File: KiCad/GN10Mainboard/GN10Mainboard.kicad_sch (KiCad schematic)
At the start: 129 parts, among them J1 USB_C_Receptacle_USB2.0_16P, J2 Conn_01x04, J3 Conn_01x04, J4 USB_C_Receptacle_USB2.0_16P, J5 Conn_01x04, J6 Conn_01x06, J7 Conn_01x04, J8 Conn_01x04, J9 XT30PW-M, SW1 SW_DIP_x04, SW2 SW_Push, SW3 SW_Push, SW4 SW_Push, SW5 SW_Push, U1 STM32G474RCTx, U10 3.3V, U2 FT231XS, U3 RNBD451, U4 FT231XS, U5 MCP2562-E-SN, U6 MCP2562-E-SN, U7 BNO055, U8 7segmentLED, U9 OKL-T/x-W5N-C, Y1 32.768kHz, Y2 24MHz, Y3 Crystal

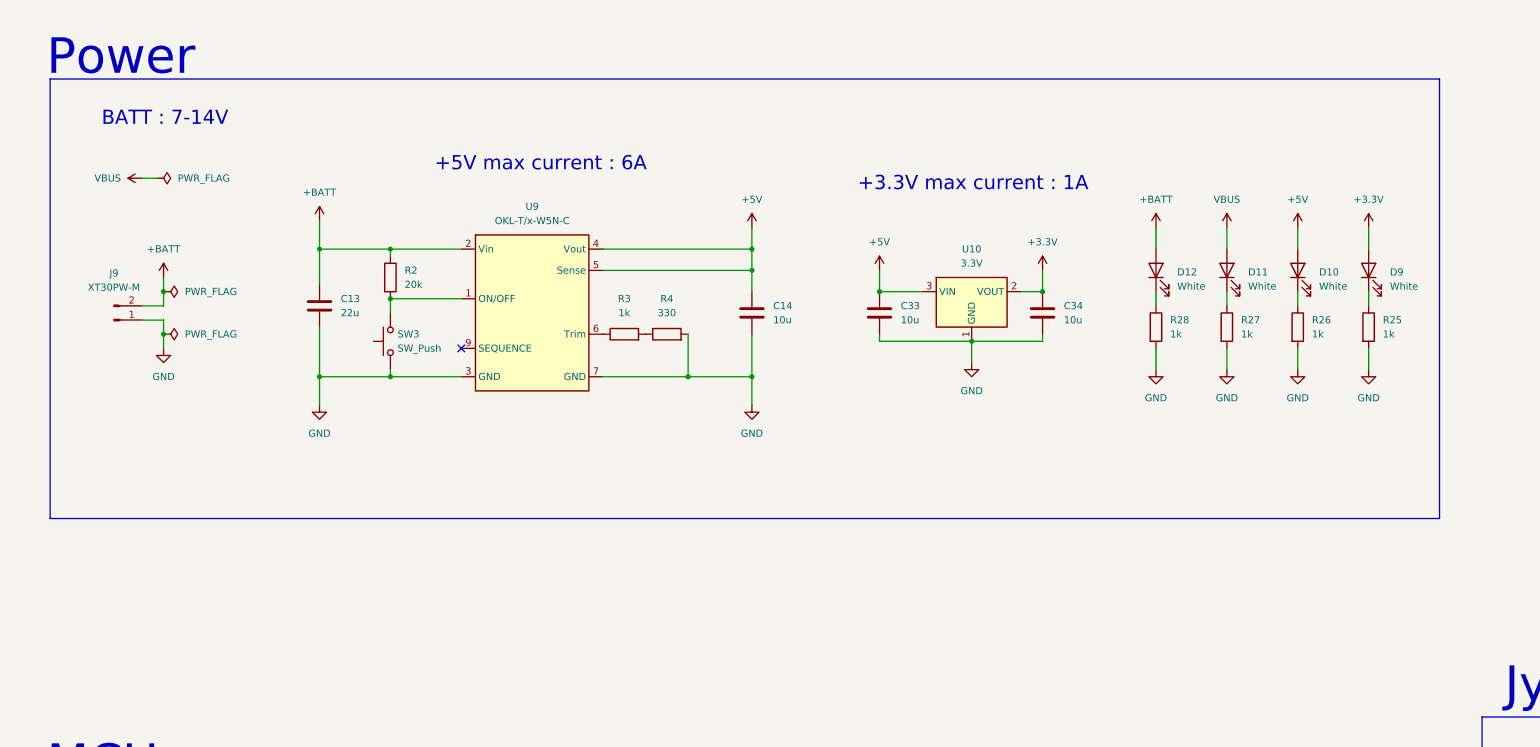
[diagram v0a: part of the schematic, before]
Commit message: add: USB power supply switch for 5V.
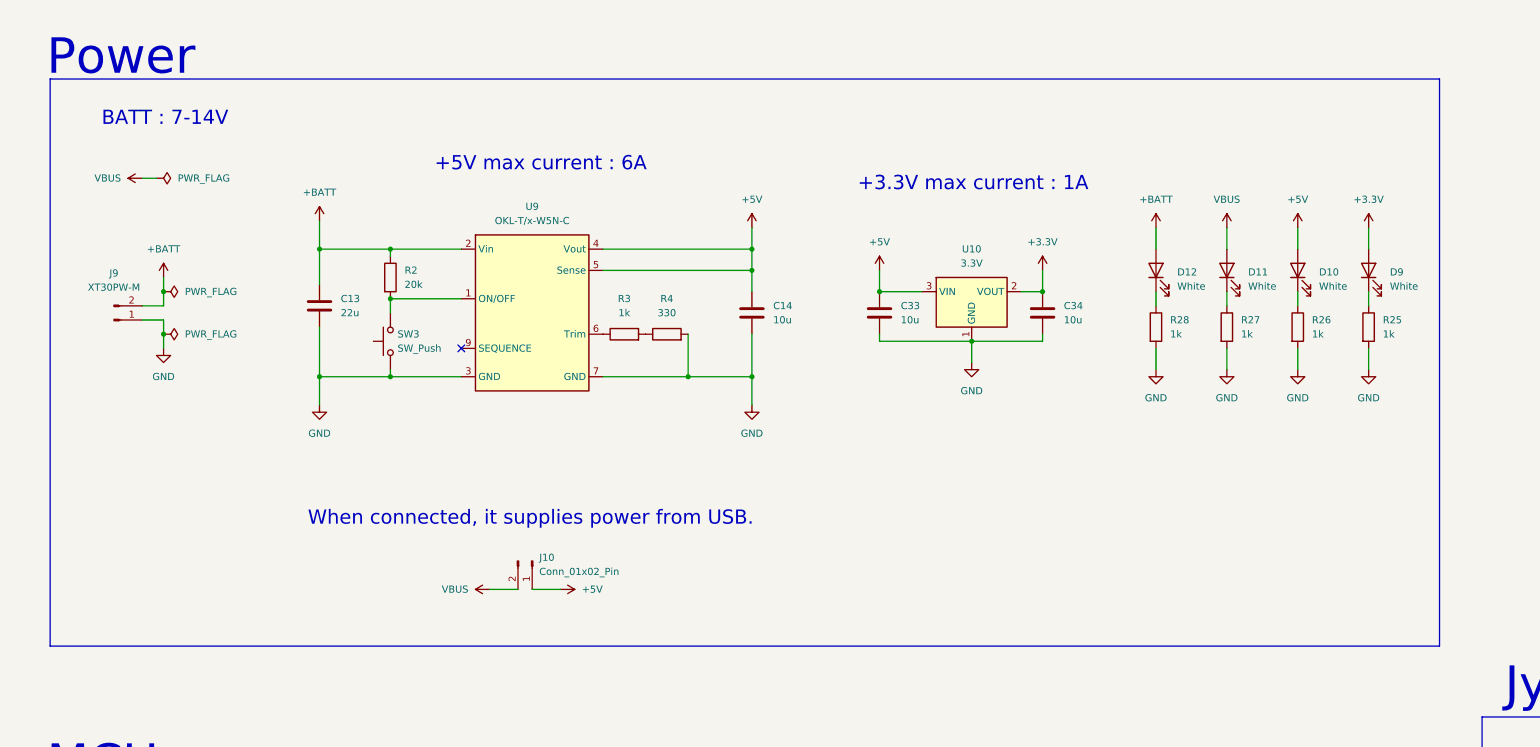
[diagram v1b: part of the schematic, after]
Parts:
- added J10: Conn_01x02_Pin, symbol Connector:Conn_01x02_Pin
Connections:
- net +5V: now also J10.1 (Pin_1)
- net VBUS: now also J10.2 (Pin_2)
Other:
- note added: "When connected, it supplies power from USB."
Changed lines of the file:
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@@
 	(wire
 		(pts
+			(xy 104.14 116.84) (xy 109.22 116.84)
+		)
+		(stroke
+			(width 0)
+			(type default)
+		)
+	)
+	(wire
+		(pts
 			(xy 118.11 171.45) (xy 128.27 171.45)
 		)
@@
 	(wire
 		(pts
+			(xy 111.76 116.84) (xy 116.84 116.84)
+		)
+		(stroke
+			(width 0)
+			(type default)
+		)
+	)
+	(wire
+		(pts
 			(xy 304.8 175.26) (xy 304.8 173.99)
 		)
@@
 	(rectangle
 		(start 25.4 25.4)
-		(end 274.32 104.14)
+		(end 274.32 127)
 		(stroke
 			(width 0)
@@
 		)
 	)
+	(text "When connected, it supplies power from USB."
+		(exclude_from_sim no)
+		(at 111.506 104.14 0)
+		(effects
+			(font
+				(size 2.54 2.54)
+			)
+		)
+	)
 	(text "MCU"
 		(exclude_from_sim no)
@@
 	)
 	(symbol
+		(lib_id "power:VBUS")
+		(at 104.14 116.84 90)
+		(unit 1)
+		(exclude_from_sim no)
+		(in_bom yes)
+		(on_board yes)
+		(dnp no)
+		(fields_autoplaced yes)
+		(property "Reference" "#PWR094"
+			(at 107.95 116.84 0)
+			(effects
+				(font
+					(size 1.27 1.27)
+				)
+				(hide yes)
+			)
+		)
+		(property "Value" "VBUS"
+			(at 100.33 116.8399 90)
+			(effects
+				(font
+					(size 1.27 1.27)
+				)
+				(justify left)
+			)
+		)
+		(property "Footprint" ""
+			(at 104.14 116.84 0)
+			(effects
+				(font
+					(size 1.27 1.27)
+				)
+				(hide yes)
+			)
+		)
+		(property "Datasheet" ""
+			(at 104.14 116.84 0)
+			(effects
+				(font
+					(size 1.27 1.27)
+				)
+				(hide yes)
+			)
+		)
+		(property "Description" "Power symbol creates a global label with name \"VBUS\""
+			(at 104.14 116.84 0)
+			(effects
+				(font
+					(size 1.27 1.27)
+				)
+				(hide yes)
+			)
+		)
+		(pin "1"
+		)
+		(instances
+			(project "GN10Mainboard"
+				(path "/b58ae320-37f1-47e7-bf16-145390e42e75"
+					(reference "#PWR094")
+					(unit 1)
+				)
+			)
+		)
+	)
+	(symbol
 		(lib_id "Device:LED")
 		(at 534.67 69.85 90)
@@
 	)
 	(symbol
+		(lib_id "Connector:Conn_01x02_Pin")
+		(at 111.76 111.76 270)
+		(unit 1)
+		(exclude_from_sim no)
+		(in_bom yes)
+		(on_board yes)
+		(dnp no)
+		(fields_autoplaced yes)
+		(property "Reference" "J10"
+			(at 113.03 111.1249 90)
+			(effects
+				(font
+					(size 1.27 1.27)
+				)
+				(justify left)
+			)
+		)
+		(property "Value" "Conn_01x02_Pin"
+			(at 113.03 113.6649 90)
+			(effects
+				(font
+					(size 1.27 1.27)
+				)
+				(justify left)
+			)
+		)
+		(property "Footprint" ""
+			(at 111.76 111.76 0)
+			(effects
+				(font
+					(size 1.27 1.27)
+				)
+				(hide yes)
+			)
+		)
+		(property "Datasheet" "~"
+			(at 111.76 111.76 0)
+			(effects
+				(font
+					(size 1.27 1.27)
+				)
+				(hide yes)
+			)
+		)
+		(property "Description" "Generic connector, single row, 01x02, script generated"
+			(at 111.76 111.76 0)
+			(effects
+				(font
+					(size 1.27 1.27)
+				)
+				(hide yes)
+			)
+		)
+		(pin "2"
+		)
+		(pin "1"
+		)
+		(instances
+			(project ""
+				(path "/b58ae320-37f1-47e7-bf16-145390e42e75"
+					(reference "J10")
+					(unit 1)
+				)
+			)
+		)
+	)
+	(symbol
 		(lib_id "power:GND")
 		(at 304.8 187.96 0)
@@
 					(unit 1)
 				)
+			)
+		)
+	)
+	(symbol
+		(lib_id "power:+5V")
+		(at 116.84 116.84 270)
+		(unit 1)
+		(exclude_from_sim no)
+		(in_bom yes)
+		(on_board yes)
+		(dnp no)
+		(fields_autoplaced yes)
+		(property "Reference" "#PWR095"
+			(at 113.03 116.84 0)
+			(effects
+				(font
+					(size 1.27 1.27)
+				)
+				(hide yes)
+			)
+		)
+		(property "Value" "+5V"
+			(at 120.65 116.8399 90)
+			(effects
+				(font
+					(size 1.27 1.27)
+				)
+				(justify left)
+			)
+		)
+		(property "Footprint" ""
+			(at 116.84 116.84 0)
+			(effects
+				(font
+					(size 1.27 1.27)
+				)
+				(hide yes)
+			)
+		)
+		(property "Datasheet" ""
+			(at 116.84 116.84 0)
+			(effects
+				(font
+					(size 1.27 1.27)
+				)
+				(hide yes)
+			)
+		)
+		(property "Description" "Power symbol creates a global label with name \"+5V\""
+			(at 116.84 116.84 0)
+			(effects
+				(font
+					(size 1.27 1.27)
+				)
+				(hide yes)
+			)
+		)
+		(pin "1"
+		)
+		(instances
+			(project "GN10Mainboard"
+				(path "/b58ae320-37f1-47e7-bf16-145390e42e75"
+					(reference "#PWR095")
+					(unit 1)
+				)

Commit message: fix: around DCDC convertor
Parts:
- removed SW3: SW_Push, symbol Switch:SW_Push
- added D17: SS2040FL, symbol Device:D
- added JP14: Jumper_2_Open, symbol Jumper:Jumper_2_Open
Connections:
- net +5V: now also D17.2 (A)
- net +BATT: now also D17.1 (K)
- net GND: now also JP14.1 (A)
- net at R2.2, U9.1 (ON/OFF): now also JP14.2 (B)
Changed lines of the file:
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@@
 	)
 	(junction
+		(at 73.66 44.45)
+		(diameter 0)
+		(color 0 0 0 0)
+	)
+	(junction
 		(at 469.9 238.76)
 		(diameter 0)
@@
 	)
 	(junction
+		(at 151.13 44.45)
+		(diameter 0)
+		(color 0 0 0 0)
+	)
+	(junction
 		(at 359.41 246.38)
 		(diameter 0)
@@
 	(wire
 		(pts
+			(xy 73.66 44.45) (xy 107.95 44.45)
+		)
+		(stroke
+			(width 0)
+			(type default)
+		)
+	)
+	(wire
+		(pts
 			(xy 419.1 361.95) (xy 431.8 361.95)
 		)
@@
 	(wire
 		(pts
+			(xy 73.66 44.45) (xy 73.66 55.88)
+		)
+		(stroke
+			(width 0)
+			(type default)
+		)
+	)
+	(wire
+		(pts
 			(xy 275.59 369.57) (xy 275.59 351.79)
 		)
@@
 	(wire
 		(pts
-			(xy 73.66 50.8) (xy 73.66 55.88)
+			(xy 73.66 40.64) (xy 73.66 44.45)
 		)
 		(stroke
@@
 	(wire
 		(pts
+			(xy 151.13 44.45) (xy 151.13 55.88)
+		)
+		(stroke
+			(width 0)
+			(type default)
+		)
+	)
+	(wire
+		(pts
 			(xy 391.16 269.24) (xy 391.16 270.51)
 		)
@@
 	(wire
 		(pts
+			(xy 115.57 44.45) (xy 151.13 44.45)
+		)
+		(stroke
+			(width 0)
+			(type default)
+		)
+	)
+	(wire
+		(pts
 			(xy 466.09 260.35) (xy 467.36 260.35)
 		)
@@
 	(wire
 		(pts
-			(xy 151.13 52.07) (xy 151.13 55.88)
+			(xy 151.13 40.64) (xy 151.13 44.45)
 		)
 		(stroke
@@
 	(text "+5V max current : 6A"
 		(exclude_from_sim no)
-		(at 113.284 40.64 0)
+		(at 112.014 31.242 0)
 		(effects
 			(font
@@
 	)
 	(symbol
-		(lib_id "Switch:SW_Push")
-		(at 86.36 72.39 90)
-		(unit 1)
-		(exclude_from_sim no)
-		(in_bom yes)
-		(on_board yes)
-		(dnp no)
-		(property "Reference" "SW3"
-			(at 87.63 71.1199 90)
-			(effects
-				(font
-					(size 1.27 1.27)
-				)
-				(justify right)
-			)
-		)
-		(property "Value" "SW_Push"
-			(at 87.63 73.6599 90)
-			(effects
-				(font
-					(size 1.27 1.27)
-				)
-				(justify right)
-			)
-		)
-		(property "Footprint" ""
-			(at 81.28 72.39 0)
-			(effects
-				(font
-					(size 1.27 1.27)
-				)
-				(hide yes)
-			)
-		)
-		(property "Datasheet" "~"
-			(at 81.28 72.39 0)
-			(effects
-				(font
-					(size 1.27 1.27)
-				)
-				(hide yes)
-			)
-		)
-		(property "Description" "Push button switch, generic, two pins"
-			(at 86.36 72.39 0)
-			(effects
-				(font
-					(size 1.27 1.27)
-				)
-				(hide yes)
-			)
-		)
-		(pin "2"
-		)
-		(pin "1"
-		)
-		(instances
-			(project ""
-				(path "/b58ae320-37f1-47e7-bf16-145390e42e75"
-					(reference "SW3")
-					(unit 1)
-				)
-			)
-		)
-	)
-	(symbol
 		(lib_id "Device:C")
 		(at 356.87 82.55 0)
@@
 	(symbol
 		(lib_id "power:+5V")
-		(at 151.13 52.07 0)
+		(at 151.13 40.64 0)
 		(unit 1)
 		(exclude_from_sim no)
@@
 		(fields_autoplaced yes)
 		(property "Reference" "#PWR022"
-			(at 151.13 55.88 0)
+			(at 151.13 44.45 0)
 			(effects
 				(font
@@
 		)
 		(property "Value" "+5V"
-			(at 151.13 46.99 0)
+			(at 151.13 35.56 0)
 			(effects
 				(font
@@
 		)
 		(property "Footprint" ""
-			(at 151.13 52.07 0)
+			(at 151.13 40.64 0)
 			(effects
 				(font
@@
 		)
 		(property "Datasheet" ""
-			(at 151.13 52.07 0)
+			(at 151.13 40.64 0)
 			(effects
 				(font
@@
 		)
 		(property "Description" "Power symbol creates a global label with name \"+5V\""
-			(at 151.13 52.07 0)
+			(at 151.13 40.64 0)
 			(effects
 				(font
@@
 	)
 	(symbol
+		(lib_id "Jumper:Jumper_2_Open")
+		(at 86.36 72.39 90)
+		(unit 1)
+		(exclude_from_sim yes)
+		(in_bom yes)
+		(on_board yes)
+		(dnp no)
+		(fields_autoplaced yes)
+		(property "Reference" "JP14"
+			(at 87.63 71.1199 90)
+			(effects
+				(font
+					(size 1.27 1.27)
+				)
+				(justify right)
+			)
+		)
+		(property "Value" "Jumper_2_Open"
+			(at 87.63 73.6599 90)
+			(effects
+				(font
+					(size 1.27 1.27)
+				)
+				(justify right)
+				(hide yes)
+			)
+		)
+		(property "Footprint" ""
+			(at 86.36 72.39 0)
+			(effects
+				(font
+					(size 1.27 1.27)
+				)
+				(hide yes)
+			)
+		)
+		(property "Datasheet" "~"
+			(at 86.36 72.39 0)
+			(effects
+				(font
+					(size 1.27 1.27)
+				)
+				(hide yes)
+			)
+		)
+		(property "Description" "Jumper, 2-pole, open"
+			(at 86.36 72.39 0)
+			(effects
+				(font
+					(size 1.27 1.27)
+				)
+				(hide yes)
+			)
+		)
+		(pin "2"
+		)
+		(pin "1"
+		)
+		(instances
+			(project "GN10Mainboard"
+				(path "/b58ae320-37f1-47e7-bf16-145390e42e75"
+					(reference "JP14")
+					(unit 1)
+				)
+			)
+		)
+	)
+	(symbol
 		(lib_id "Jumper:SolderJumper_2_Open")
 		(at 488.95 182.88 0)
@@
 	(symbol
 		(lib_id "power:+BATT")
-		(at 73.66 50.8 0)
+		(at 73.66 40.64 0)
 		(unit 1)
 		(exclude_from_sim no)
@@
 		(fields_autoplaced yes)
 		(property "Reference" "#PWR020"
-			(at 73.66 54.61 0)
+			(at 73.66 44.45 0)
 			(effects
 				(font
@@
 		)
 		(property "Value" "+BATT"
-			(at 73.66 45.72 0)
+			(at 73.66 35.56 0)
 			(effects
 				(font
@@
 		)
 		(property "Footprint" ""
-			(at 73.66 50.8 0)
+			(at 73.66 40.64 0)
 			(effects
 				(font
@@
 		)
 		(property "Datasheet" ""
-			(at 73.66 50.8 0)
+			(at 73.66 40.64 0)
 			(effects
 				(font
@@
 		)
 		(property "Description" "Power symbol creates a global label with name \"+BATT\""
-			(at 73.66 50.8 0)
+			(at 73.66 40.64 0)
 			(effects
 				(font
@@
 					(unit 1)
 				)
+			)
+		)
+	)
+	(symbol
+		(lib_id "Device:D")
+		(at 111.76 44.45 0)
+		(unit 1)
+		(exclude_from_sim no)
+		(in_bom yes)
+		(on_board yes)
+		(dnp no)
+		(fields_autoplaced yes)
+		(property "Reference" "D17"
+			(at 111.76 38.1 0)
+			(effects
+				(font
+					(size 1.27 1.27)
+				)
+			)
+		)
+		(property "Value" "SS2040FL"
+			(at 111.76 40.64 0)
+			(effects
+				(font
+					(size 1.27 1.27)
+				)
+			)
+		)
+		(property "Footprint" ""
+			(at 111.76 44.45 0)
+			(effects
+				(font
+					(size 1.27 1.27)
+				)
+				(hide yes)
+			)
+		)
+		(property "Datasheet" "~"
+			(at 111.76 44.45 0)
+			(effects
+				(font
+					(size 1.27 1.27)
+				)
+				(hide yes)
+			)
+		)
+		(property "Description" "Diode"
+			(at 111.76 44.45 0)
+			(effects
+				(font
+					(size 1.27 1.27)
+				)
+				(hide yes)
+			)
+		)
+		(property "Sim.Device" "D"
+			(at 111.76 44.45 0)
+			(effects
+				(font
+					(size 1.27 1.27)
+				)
+				(hide yes)
+			)
+		)
+		(property "Sim.Pins" "1=K 2=A"
+			(at 111.76 44.45 0)
+			(effects
+				(font
+					(size 1.27 1.27)
+				)
+				(hide yes)
+			)
+		)
+		(pin "2"
+		)
+		(pin "1"
+		)
+		(instances
+			(project ""
+				(path "/b58ae320-37f1-47e7-bf16-145390e42e75"
+					(reference "D17")
+					(unit 1)
+				)

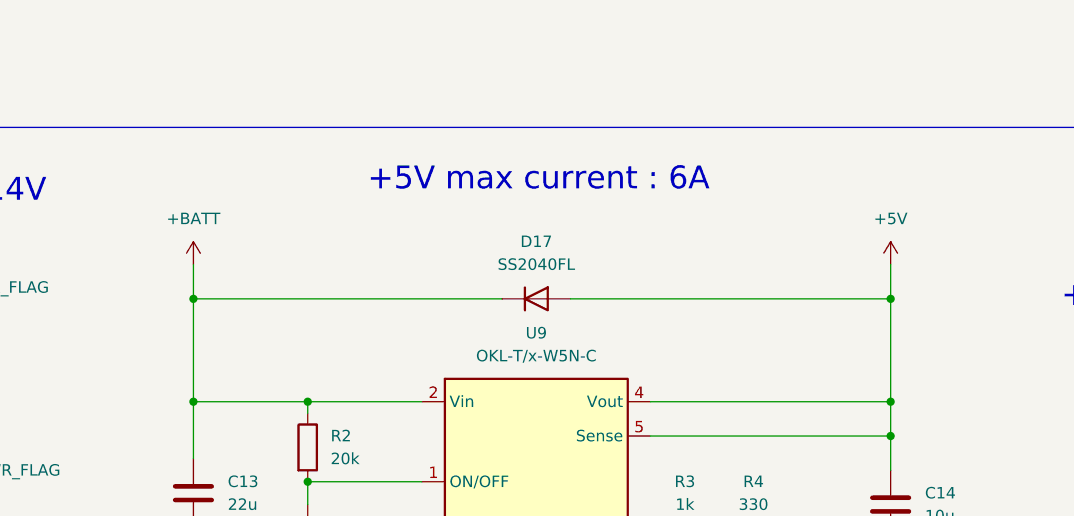
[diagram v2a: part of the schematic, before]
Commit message: The DCDC does not require a reverse voltage protection diode, so I removed it.
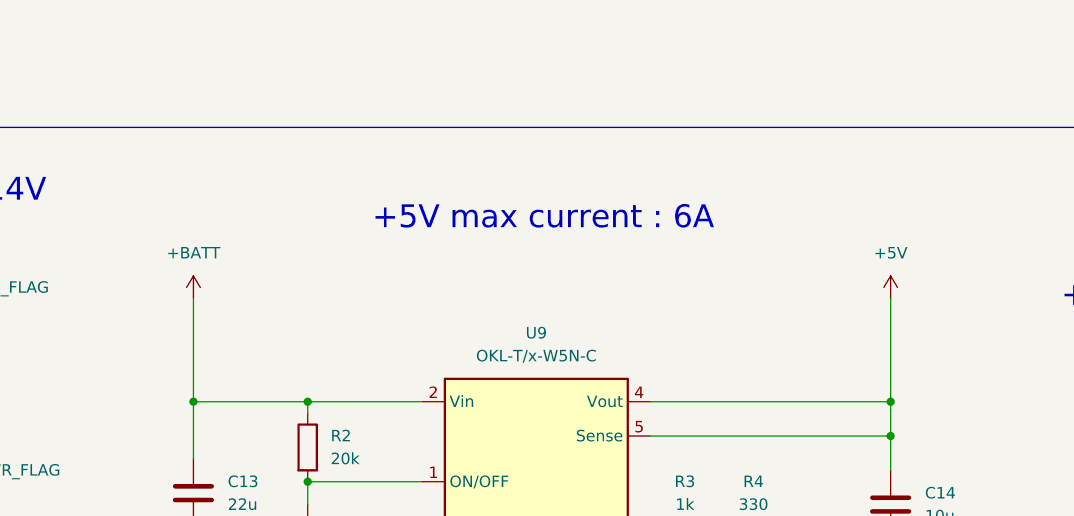
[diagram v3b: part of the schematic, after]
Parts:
- removed D17: SS2040FL, symbol Device:D
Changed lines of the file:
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@@
 	)
 	(junction
-		(at 73.66 44.45)
-		(diameter 0)
-		(color 0 0 0 0)
-	)
-	(junction
 		(at 469.9 238.76)
 		(diameter 0)
@@
 	)
 	(junction
-		(at 151.13 44.45)
-		(diameter 0)
-		(color 0 0 0 0)
-	)
-	(junction
 		(at 359.41 246.38)
 		(diameter 0)
@@
 	(wire
 		(pts
-			(xy 73.66 44.45) (xy 107.95 44.45)
-		)
-		(stroke
-			(width 0)
-			(type default)
-		)
-	)
-	(wire
-		(pts
 			(xy 419.1 361.95) (xy 431.8 361.95)
 		)
@@
 	(wire
 		(pts
-			(xy 73.66 40.64) (xy 73.66 44.45)
-		)
-		(stroke
-			(width 0)
-			(type default)
-		)
-	)
-	(wire
-		(pts
 			(xy 491.49 260.35) (xy 494.03 260.35)
 		)
@@
 	(wire
 		(pts
-			(xy 115.57 44.45) (xy 151.13 44.45)
-		)
-		(stroke
-			(width 0)
-			(type default)
-		)
-	)
-	(wire
-		(pts
 			(xy 466.09 260.35) (xy 467.36 260.35)
 		)
@@
 	(wire
 		(pts
-			(xy 151.13 40.64) (xy 151.13 44.45)
-		)
-		(stroke
-			(width 0)
-			(type default)
-		)
-	)
-	(wire
-		(pts
 			(xy 466.09 236.22) (xy 466.09 238.76)
 		)
@@
 	(text "+5V max current : 6A"
 		(exclude_from_sim no)
-		(at 112.014 31.242 0)
+		(at 112.522 35.56 0)
 		(effects
 			(font
@@
 	(symbol
 		(lib_id "power:+5V")
-		(at 151.13 40.64 0)
+		(at 151.13 44.45 0)
 		(unit 1)
 		(exclude_from_sim no)
@@
 		(fields_autoplaced yes)
 		(property "Reference" "#PWR022"
-			(at 151.13 44.45 0)
+			(at 151.13 48.26 0)
 			(effects
 				(font
@@
 		)
 		(property "Value" "+5V"
-			(at 151.13 35.56 0)
+			(at 151.13 39.37 0)
 			(effects
 				(font
@@
 		)
 		(property "Footprint" ""
-			(at 151.13 40.64 0)
+			(at 151.13 44.45 0)
 			(effects
 				(font
@@
 		)
 		(property "Datasheet" ""
-			(at 151.13 40.64 0)
+			(at 151.13 44.45 0)
 			(effects
 				(font
@@
 		)
 		(property "Description" "Power symbol creates a global label with name \"+5V\""
-			(at 151.13 40.64 0)
+			(at 151.13 44.45 0)
 			(effects
 				(font
@@
 	(symbol
 		(lib_id "power:+BATT")
-		(at 73.66 40.64 0)
+		(at 73.66 44.45 0)
 		(unit 1)
 		(exclude_from_sim no)
@@
 		(fields_autoplaced yes)
 		(property "Reference" "#PWR020"
-			(at 73.66 44.45 0)
+			(at 73.66 48.26 0)
 			(effects
 				(font
@@
 		)
 		(property "Value" "+BATT"
-			(at 73.66 35.56 0)
+			(at 73.66 39.37 0)
 			(effects
 				(font
@@
 		)
 		(property "Footprint" ""
-			(at 73.66 40.64 0)
+			(at 73.66 44.45 0)
 			(effects
 				(font
@@
 		)
 		(property "Datasheet" ""
-			(at 73.66 40.64 0)
+			(at 73.66 44.45 0)
 			(effects
 				(font
@@
 		)
 		(property "Description" "Power symbol creates a global label with name \"+BATT\""
-			(at 73.66 40.64 0)
+			(at 73.66 44.45 0)
 			(effects
 				(font
@@
 					(unit 1)
 				)
-			)
-		)
-	)
-	(symbol
-		(lib_id "Device:D")
-		(at 111.76 44.45 0)
-		(unit 1)
-		(exclude_from_sim no)
-		(in_bom yes)
-		(on_board yes)
-		(dnp no)
-		(fields_autoplaced yes)
-		(property "Reference" "D17"
-			(at 111.76 38.1 0)
-			(effects
-				(font
-					(size 1.27 1.27)
-				)
-			)
-		)
-		(property "Value" "SS2040FL"
-			(at 111.76 40.64 0)
-			(effects
-				(font
-					(size 1.27 1.27)
-				)
-			)
-		)
-		(property "Footprint" ""
-			(at 111.76 44.45 0)
-			(effects
-				(font
-					(size 1.27 1.27)
-				)
-				(hide yes)
-			)
-		)
-		(property "Datasheet" "~"
-			(at 111.76 44.45 0)
-			(effects
-				(font
-					(size 1.27 1.27)
-				)
-				(hide yes)
-			)
-		)
-		(property "Description" "Diode"
-			(at 111.76 44.45 0)
-			(effects
-				(font
-					(size 1.27 1.27)
-				)
-				(hide yes)
-			)
-		)
-		(property "Sim.Device" "D"
-			(at 111.76 44.45 0)
-			(effects
-				(font
-					(size 1.27 1.27)
-				)
-				(hide yes)
-			)
-		)
-		(property "Sim.Pins" "1=K 2=A"
-			(at 111.76 44.45 0)
-			(effects
-				(font
-					(size 1.27 1.27)
-				)
-				(hide yes)
-			)
-		)
-		(pin "2"
-		)
-		(pin "1"
-		)
-		(instances
-			(project ""
-				(path "/b58ae320-37f1-47e7-bf16-145390e42e75"
-					(reference "D17")
-					(unit 1)
-				)
